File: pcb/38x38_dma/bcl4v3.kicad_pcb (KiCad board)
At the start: 2 copper layers, 38 x 38 mm, 34 parts, among them J1 Conn_01x04, J10 Conn_01x04, J2 Conn_01x04, J3 Conn_01x04, J4 Conn_01x04, J5 Conn_01x04, J6 Conn_01x04, J7 Conn_01x04, J8 Conn_01x04, J9 10118194-0001LF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

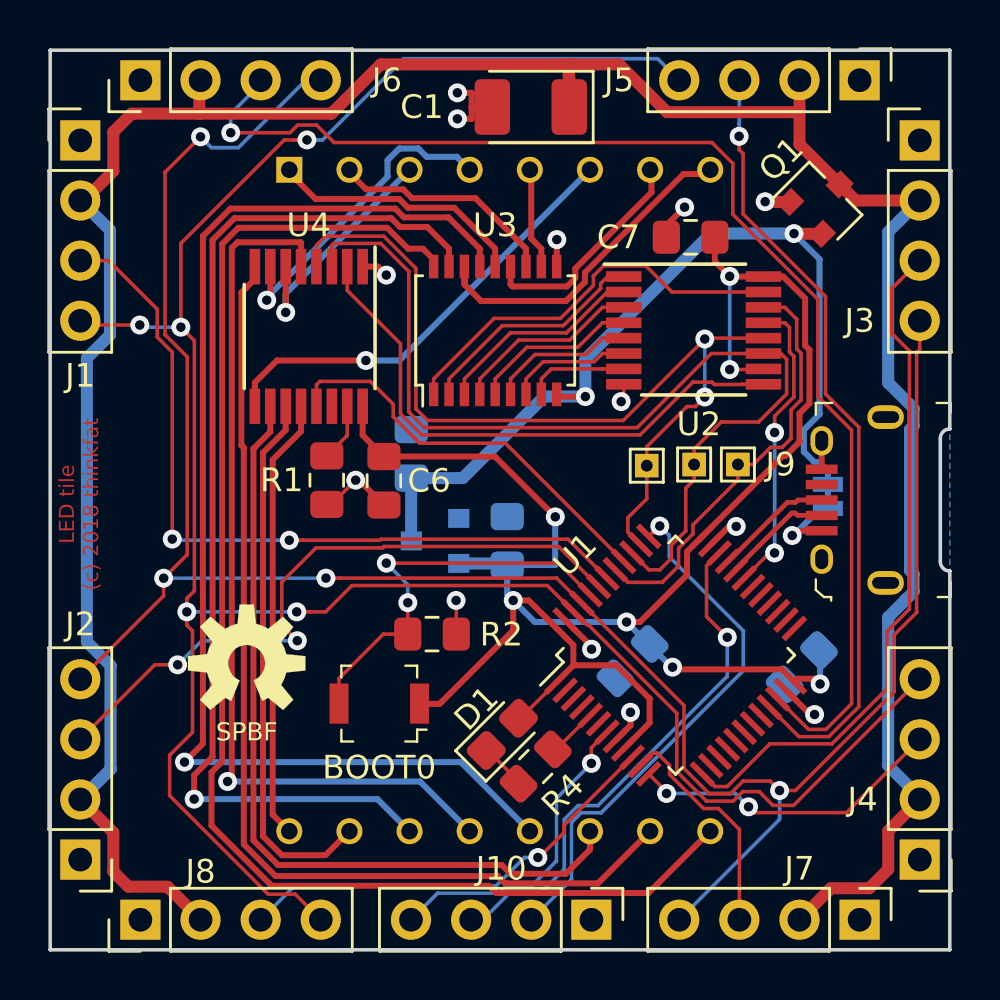
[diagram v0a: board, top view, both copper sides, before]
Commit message: PCB updates: 32kHz oscillator, separate VBAT supply
also, longer pads for the row driver
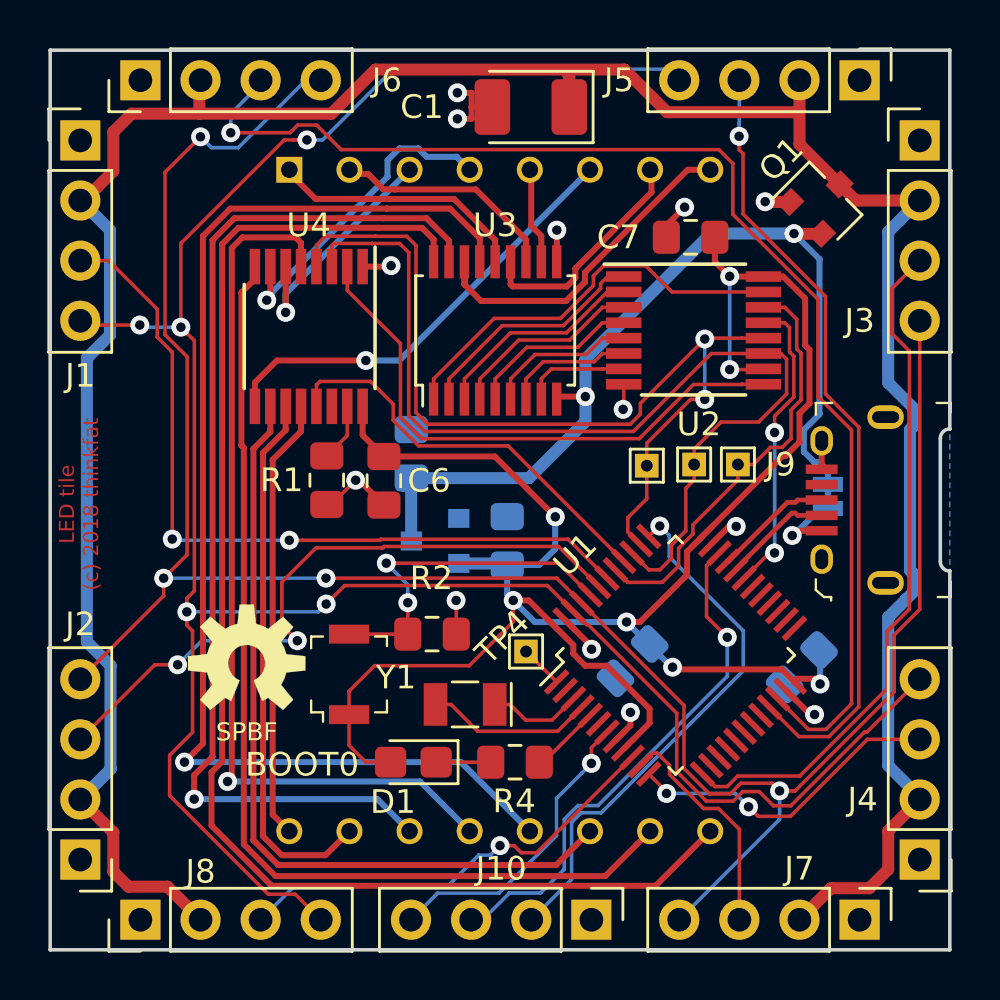
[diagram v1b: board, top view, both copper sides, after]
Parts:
- added TP4: TestPoint, TestPoint:TestPoint_THTPad_1.0x1.0mm_Drill0.5mm, F.Cu at (134.1, 89.4)
- added Y1: ABS07-120-32.768KHZ-Z, Crystal:Crystal_SMD_MicroCrystal_CC7V-T1A-2Pin_3.2x1.5mm, F.Cu at (131.5, 91.6)
- D1: value LED -> SM0805HCL
- moved D1 3.94 mm to (129.3, 94.1), turned to 180 degrees
- moved BOOT0 1.77 mm to (126.6, 90.4), turned to 90 degrees
- moved R4 0.89 mm to (133.6, 94.1), turned to 0 degrees
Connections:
- U1 pad 1: +3V3 -> /VBAT
- U1 pad 3: Net-(U1-Pad3) -> /OSC_IN
- U1 pad 4: Net-(U1-Pad4) -> /OSC_OUT
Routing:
- net /OSC_OUT: track 0.00 -> 7.07 mm
- net /OSC_IN: track 0.00 -> 3.97 mm
- net +3V3: track 83.0 -> 86.0 mm
- net /BOOT0: track 17.3 -> 15.0 mm
- net /VBAT: track 0.00 -> 1.83 mm
- net /CAT_STROBE: track 38.5 -> 39.7 mm
- net /LED: track 2.17 -> 2.97 mm
- net /COL_6: track 34.6 -> 33.9 mm
- net GND: track 20.8 -> 21.5 mm
- net /CAT_CLK: track 41.7 -> 42.4 mm
- net /nRST: track 13.5 -> 12.9 mm
- net +5V: track 38.4 -> 39.0 mm
